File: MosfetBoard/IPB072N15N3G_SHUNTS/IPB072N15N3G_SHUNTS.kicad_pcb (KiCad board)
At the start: 2 copper layers, 120 x 75 mm, 81 parts, among them J1 DRIVER1, J14 BATT-Conn2, J2 DRIVER1, J3 DRIVER1, J4 PhaseConn, J5 PhaseConn, J6 PhaseConn, J9 BATT-Conn1, Q1 IPB072N15N3G, Q10 IPB072N15N3G, Q11 IPB072N15N3G, Q12 IPB072N15N3G, Q2 IPB072N15N3G, Q3 IPB072N15N3G, Q4 IPB072N15N3G, Q5 IPB072N15N3G, Q6 IPB072N15N3G, Q7 IPB072N15N3G, Q8 IPB072N15N3G, Q9 IPB072N15N3G

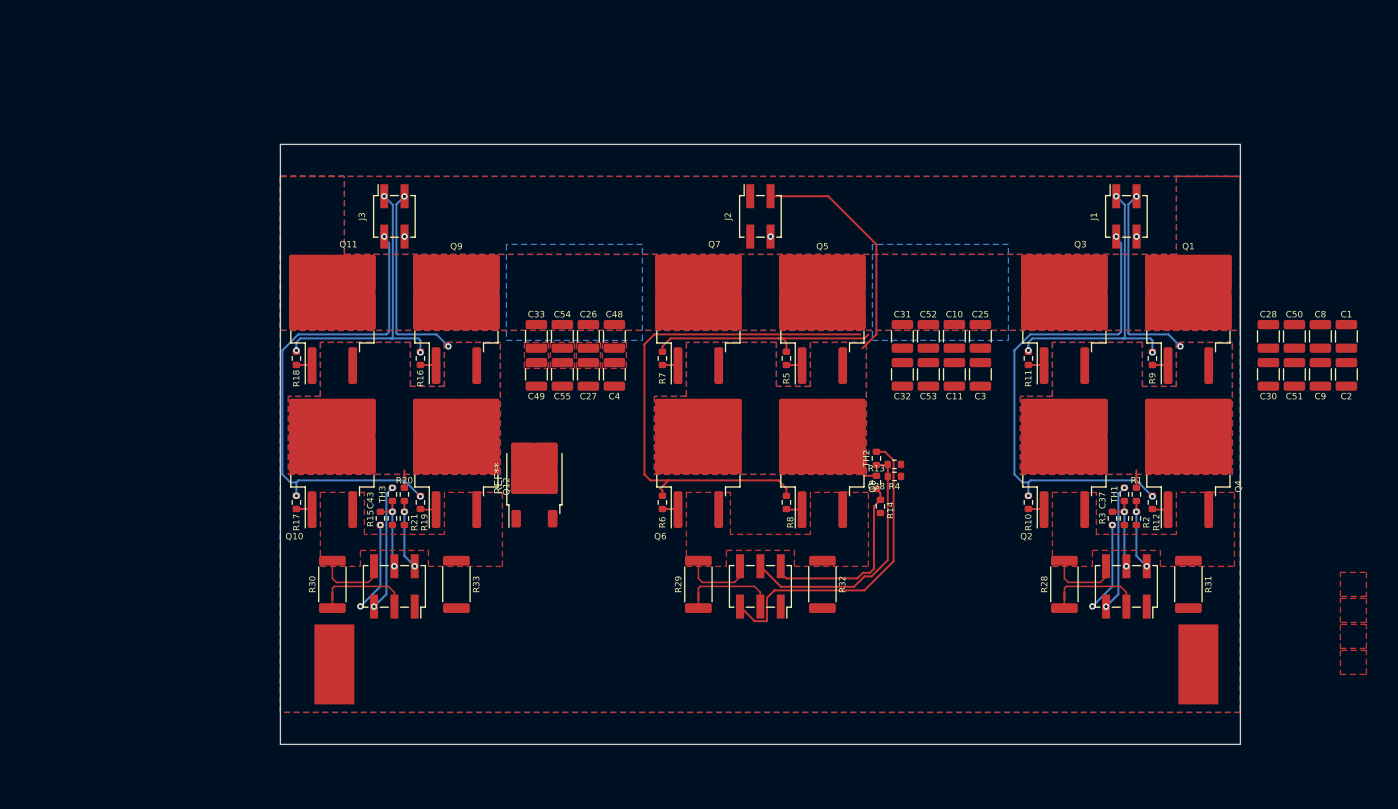
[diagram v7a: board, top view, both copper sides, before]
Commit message: v2.8.0 - Small Hall sensors
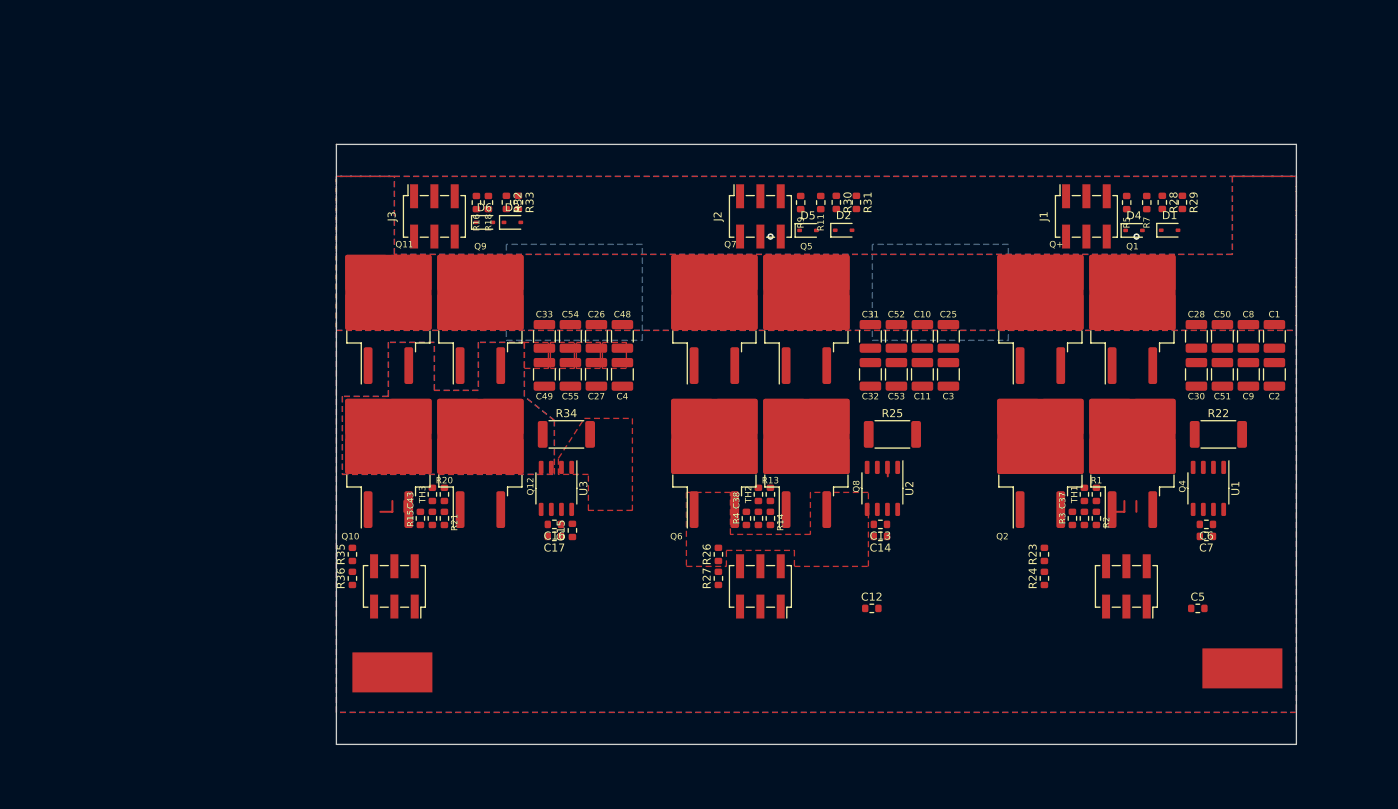
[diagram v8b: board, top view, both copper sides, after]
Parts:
- removed JP1, JP2, JP3: DummyJumper, GigaVescLibs:SolderJumper0.3mm
- removed R10, R12, R17, R19, R6, R8: 2.2, Resistor_SMD:R_0603_1608Metric
- removed REF**: TO-252-2, Package_TO_SOT_SMD:TO-252-2
- added C12: 100n, GigaVescLibs:C_0603_1608Metric_L, F.Cu at (169.9, 112.0)
- added C13: 10n, GigaVescLibs:C_0603_1608Metric_L, F.Cu at (171.0, 101.5)
- added C14: 1n, GigaVescLibs:C_0603_1608Metric_L, F.Cu at (171.0, 103.0)
- added C15: 100n, GigaVescLibs:C_0603_1608Metric_L, F.Cu at (132.5, 102.2)
- added C16: 10n, GigaVescLibs:C_0603_1608Metric_L, F.Cu at (130.2, 101.5)
- added C17: 1n, GigaVescLibs:C_0603_1608Metric_L, F.Cu at (130.2, 103.0)
- added C5: 100n, GigaVescLibs:C_0603_1608Metric_L, F.Cu at (210.7, 112.0)
- added C6: 10n, GigaVescLibs:C_0603_1608Metric_L, F.Cu at (211.8, 101.5)
- added C7: 1n, GigaVescLibs:C_0603_1608Metric_L, F.Cu at (211.8, 103.0)
- added D1: 1N5819WS, Diode_SMD:D_SOD-323, F.Cu at (207.2, 64.7)
- added D2: 1N5819WS, Diode_SMD:D_SOD-323, F.Cu at (166.4, 64.7)
- added D3: 1N5819WS, Diode_SMD:D_SOD-323, F.Cu at (125.0, 63.8)
- added D4: 1N5819WS, Diode_SMD:D_SOD-323, F.Cu at (202.7, 64.8)
- added D5: 1N5819WS, Diode_SMD:D_SOD-323, F.Cu at (161.9, 64.8)
- added D6: 1N5819WS, Diode_SMD:D_SOD-323, F.Cu at (121.5, 63.8)
- added R22: 0.3m, Resistor_SMD:R_2512_6332Metric, F.Cu at (213.2, 90.2)
- added R23: 4.7k, Resistor_SMD:R_0603_1608Metric, F.Cu at (191.5, 105.2)
- added R24: 9.1k, Resistor_SMD:R_0603_1608Metric, F.Cu at (191.5, 108.2)
- added R25: 0.3m, Resistor_SMD:R_2512_6332Metric, F.Cu at (172.5, 90.2)
- added R26: 4.7k, Resistor_SMD:R_0603_1608Metric, F.Cu at (150.8, 105.2)
- added R27: 9.1k, Resistor_SMD:R_0603_1608Metric, F.Cu at (150.8, 108.2)
- added R34: 0.3m, Resistor_SMD:R_2512_6332Metric, F.Cu at (131.8, 90.2)
- added R35: 4.7k, Resistor_SMD:R_0603_1608Metric, F.Cu at (105.0, 105.2)
- added R36: 9.1k, Resistor_SMD:R_0603_1608Metric, F.Cu at (105.0, 108.2)
- added U1: MT9223CT-50BR5, Package_SO:SOP-8_3.9x4.9mm_P1.27mm, F.Cu at (212.0, 97.0)
- added U2: MT9223CT-50BR5, Package_SO:SOP-8_3.9x4.9mm_P1.27mm, F.Cu at (171.2, 97.0)
- added U3: MT9223CT-50BR5, Package_SO:SOP-8_3.9x4.9mm_P1.27mm, F.Cu at (130.5, 97.0)
- J1, J2, J3: value DRIVER1 -> DriverConn; footprint Connector_PinSocket_2.54mm:PinSocket_2x02_P2.54mm_Vertical_SMD -> Connector_PinSocket_2.54mm:PinSocket_2x03_P2.54mm_Vertical_SMD
- R11, R18, R7: value 2.2 -> 10
- R16, R5, R9: value 2.2 -> 1
- R28, R30, R32: value 0.5m -> 1; footprint Resistor_SMD:R_2512_6332Metric -> Resistor_SMD:R_0603_1608Metric
- R29, R31, R33: value 0.5m -> 10; footprint Resistor_SMD:R_2512_6332Metric -> Resistor_SMD:R_0603_1608Metric
- moved R30 79.0 mm to (165.5, 61.2)
- moved R29 77.1 mm to (208.8, 61.2)
- moved R7 63.6 mm to (204.3, 61.3)
- moved R31 63.3 mm to (168.0, 61.2)
- moved R32 62.0 mm to (124.2, 61.2)
- moved R28 49.3 mm to (206.2, 61.2)
- moved R33 48.4 mm to (125.8, 61.2)
- moved R9 48.1 mm to (161.0, 61.3)
- moved R5 46.8 mm to (201.8, 61.3)
- moved R11 32.5 mm to (163.5, 61.3)
- moved R18 30.9 mm to (122.0, 61.3)
- moved R16 20.7 mm to (120.5, 61.3)
- moved R4 19.2 mm to (154.2, 100.8), turned to -90 degrees
- moved C38 18.3 mm to (155.8, 100.8), turned to -90 degrees
- moved TH2 15.4 mm to (155.8, 97.8)
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- renumbered Q3 to Q+
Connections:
- J1 pad 1: /PhaseMosfets1/PH -> /PhaseMosfets1/PHASE
- J1 pad 2: /PhaseMosfets1/PL -> /PhaseMosfets1/PH
- J1 pad 3: /PhaseMosfets1/PHASE -> /PhaseMosfets1/PL
- J2 pad 1: /PhaseMosfets2/PH -> /PhaseMosfets2/PHASE
- J2 pad 2: /PhaseMosfets2/PL -> /PhaseMosfets2/PH
- J2 pad 3: /PhaseMosfets2/PHASE -> /PhaseMosfets2/PL
- J3 pad 1: /PhaseMosfets3/PH -> /PhaseMosfets3/PHASE
- J3 pad 2: /PhaseMosfets3/PL -> /PhaseMosfets3/PH
- J3 pad 3: /PhaseMosfets3/PHASE -> /PhaseMosfets3/PL
- J4 pad 1: -BATT -> /PhaseMosfets1/5V_IN
- J4 pad 3: /PhaseMosfets1/SH- -> GNDA
- J5 pad 1: -BATT -> /PhaseMosfets2/5V_IN
- J5 pad 3: /PhaseMosfets2/SH- -> GNDA
- J6 pad 1: -BATT -> /PhaseMosfets3/5V_IN
- J6 pad 3: /PhaseMosfets3/SH- -> GNDA
- Q+ pad 1: Net-(Q3-G) -> /PhaseMosfets1/HIGH
- Q1 pad 1: Net-(Q1-G) -> /PhaseMosfets1/HIGH
- Q10 pad 1: Net-(Q10-G) -> /PhaseMosfets3/LOW
- Q10 pad 3: /PhaseMosfets3/SH+ -> -BATT
- Q11 pad 1: Net-(Q11-G) -> /PhaseMosfets3/HIGH
- Q12 pad 1: Net-(Q12-G) -> /PhaseMosfets3/LOW
- Q12 pad 3: /PhaseMosfets3/SH+ -> -BATT
- Q2 pad 1: Net-(Q2-G) -> /PhaseMosfets1/LOW
- Q2 pad 3: /PhaseMosfets1/SH+ -> -BATT
- Q4 pad 1: Net-(Q4-G) -> /PhaseMosfets1/LOW
- Q4 pad 3: /PhaseMosfets1/SH+ -> -BATT
- Q5 pad 1: Net-(Q5-G) -> /PhaseMosfets2/HIGH
- Q6 pad 1: Net-(Q6-G) -> /PhaseMosfets2/LOW
- Q6 pad 3: /PhaseMosfets2/SH+ -> -BATT
- Q7 pad 1: Net-(Q7-G) -> /PhaseMosfets2/HIGH
- Q8 pad 1: Net-(Q8-G) -> /PhaseMosfets2/LOW
- Q8 pad 3: /PhaseMosfets2/SH+ -> -BATT
- Q9 pad 1: Net-(Q9-G) -> /PhaseMosfets3/HIGH
- R1 pad 1: /PhaseMosfets1/PHASE -> /PhaseMosfets1/PHASE_OUT
- R11 pad 1: /PhaseMosfets1/PH -> /PhaseMosfets2/PL
- R11 pad 2: Net-(Q3-G) -> /PhaseMosfets2/LOW
- R13 pad 1: /PhaseMosfets2/PHASE -> /PhaseMosfets2/PHASE_OUT
- R16 pad 1: /PhaseMosfets3/PH -> /PhaseMosfets3/PL
- R16 pad 2: Net-(Q9-G) -> Net-(D6-K)
- R18 pad 1: /PhaseMosfets3/PH -> /PhaseMosfets3/PL
- R18 pad 2: Net-(Q11-G) -> /PhaseMosfets3/LOW
- R20 pad 1: /PhaseMosfets3/PHASE -> /PhaseMosfets3/PHASE_OUT
- R28 pad 1: /PhaseMosfets1/SH+ -> /PhaseMosfets1/PH
- R28 pad 2: -BATT -> Net-(D1-K)
- R29 pad 1: /PhaseMosfets2/SH+ -> /PhaseMosfets1/PH
- R29 pad 2: -BATT -> /PhaseMosfets1/HIGH
- R30 pad 1: /PhaseMosfets3/SH+ -> /PhaseMosfets2/PH
- R30 pad 2: -BATT -> Net-(D2-K)
- R31 pad 1: /PhaseMosfets1/SH+ -> /PhaseMosfets2/PH
- R31 pad 2: -BATT -> /PhaseMosfets2/HIGH
- R32 pad 1: /PhaseMosfets2/SH+ -> /PhaseMosfets3/PH
- R32 pad 2: -BATT -> Net-(D3-K)
- R33 pad 1: /PhaseMosfets3/SH+ -> /PhaseMosfets3/PH
- R33 pad 2: -BATT -> /PhaseMosfets3/HIGH
- R5 pad 1: /PhaseMosfets2/PH -> /PhaseMosfets1/PL
- R5 pad 2: Net-(Q5-G) -> Net-(D4-K)
- R7 pad 1: /PhaseMosfets2/PH -> /PhaseMosfets1/PL
- R7 pad 2: Net-(Q7-G) -> /PhaseMosfets1/LOW
- R9 pad 1: /PhaseMosfets1/PH -> /PhaseMosfets2/PL
- R9 pad 2: Net-(Q1-G) -> Net-(D5-K)
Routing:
- net /PhaseMosfets2/PL: track 65.6 -> 0.00 mm
- net /PhaseMosfets3/PL: track 62.3 -> 0.00 mm, vias 3 -> 0
- net /PhaseMosfets1/PL: track 62.3 -> 0.00 mm, vias 3 -> 0
- net /PhaseMosfets2/3.3V_IN: track 40.0 -> 0.00 mm
- net /PhaseMosfets1/PH: track 37.0 -> 0.00 mm, vias 3 -> 0
- net /PhaseMosfets3/PH: track 37.0 -> 0.00 mm, vias 3 -> 0
- net /PhaseMosfets2/PHASE: track 34.5 -> 0.00 mm
- net /PhaseMosfets2/MOS_TEMP: track 31.8 -> 0.00 mm
- net /PhaseMosfets2/PH: track 29.4 -> 0.00 mm
- net /PhaseMosfets1/PHASE: track 26.9 -> 0.00 mm, vias 2 -> 0
- net /PhaseMosfets3/PHASE: track 26.9 -> 0.00 mm, vias 2 -> 0
- net /PhaseMosfets2/V_SENSE: track 23.8 -> 0.00 mm
- net -BATT: track 22.4 -> 1.35 mm, vias 7 -> 2
- net /PhaseMosfets3/3.3V_IN: track 15.8 -> 0.00 mm, vias 2 -> 0
- net /PhaseMosfets1/3.3V_IN: track 15.8 -> 0.00 mm, vias 2 -> 0
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- added copper zone on F.Cu, net /PhaseMosfets3/PHASE_OUT
- removed copper zone on B.Cu, net /PhaseMosfets1/PHASE
- removed copper zone on F.Cu, net /PhaseMosfets1/PHASE
- removed copper zone on F.Cu, net /PhaseMosfets1/SH+
- removed copper zone on B.Cu, net /PhaseMosfets2/PHASE
- removed copper zone on F.Cu, net /PhaseMosfets2/PHASE
- removed copper zone on F.Cu, net /PhaseMosfets3/SH+
- removed copper zone on F.Cu, net Net-(C10-Pad2)
- removed copper zone on F.Cu, net Net-(C25-Pad2)
- removed copper zone on F.Cu, net Net-(C31-Pad2)
- removed copper zone on F.Cu, net Net-(C52-Pad2)
